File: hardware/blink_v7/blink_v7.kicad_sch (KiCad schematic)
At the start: 98 parts, among them J1 Conn_01x02, J14 Conn_02x16_Odd_Even, J5 Conn_01x04_Pin, J6 Conn_01x04_Pin, J7 Conn_01x06_Pin, J8 Conn_01x06, J9 USB_C_Receptacle, SW1 MK-12C02-G025, SW2 SW_SPDT, SW3 SW_SPDT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

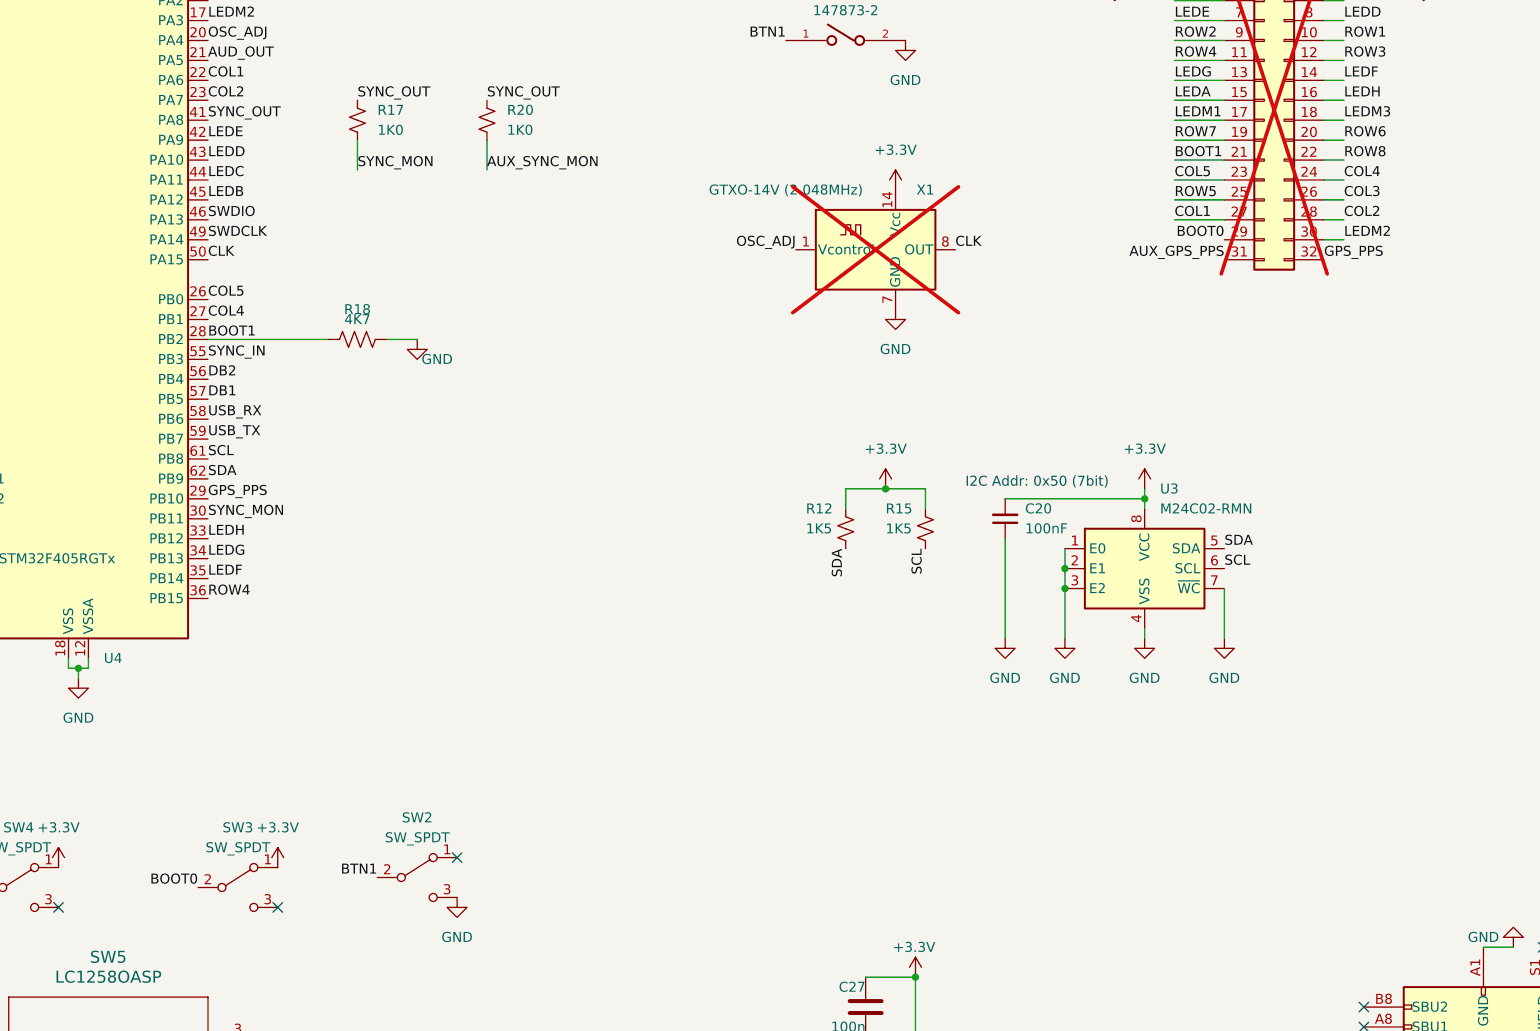
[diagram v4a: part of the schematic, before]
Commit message: main counter counting
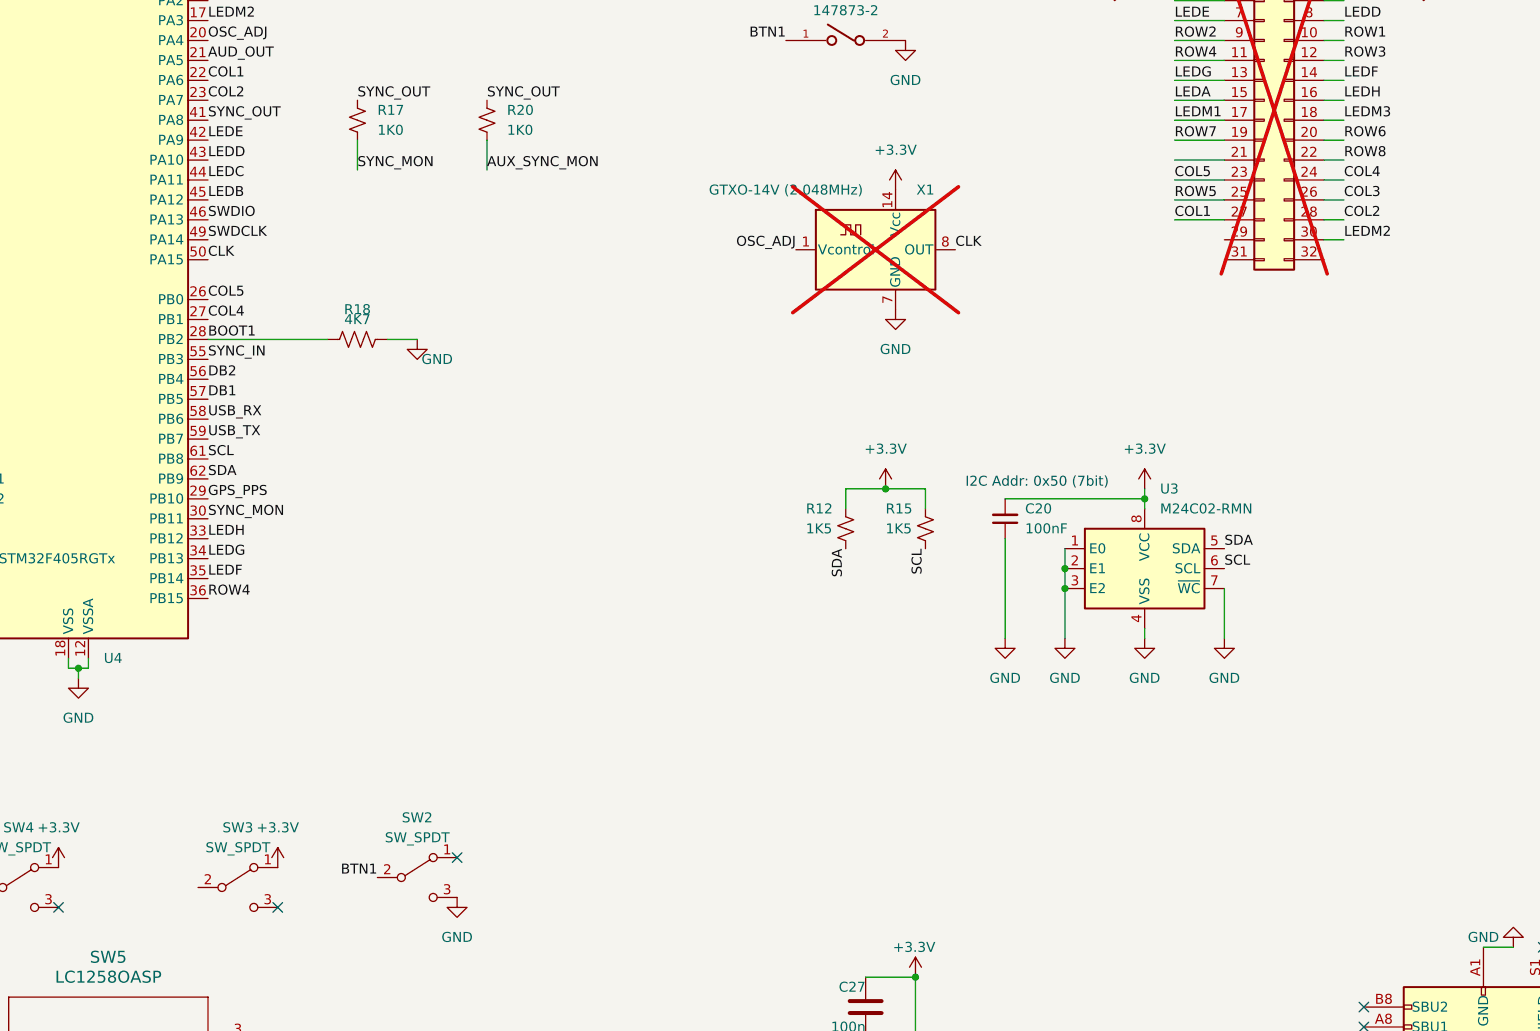
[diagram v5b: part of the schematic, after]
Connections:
- net AUX_GPS_PPS: no longer J14.31 (Pin_31)
- net BOOT0: no longer J14.29 (Pin_29), SW3.2 (B)
- net BOOT1: no longer J14.21 (Pin_21)
- net GPS_PPS: no longer J14.32 (Pin_32)
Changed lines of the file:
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@@
-    (effects (font (size 1.27 1.27)) (justify right bottom))
-  )
-  (label "AUX_GPS_PPS" (at 372.11 71.12 180) (fields_autoplaced)
     (effects (font (size 1.27 1.27)) (justify right bottom))
   )
@@
     (effects (font (size 1.27 1.27)) (justify left bottom))
   )
-  (label "BOOT0" (at 372.11 68.58 180) (fields_autoplaced)
-    (effects (font (size 1.27 1.27)) (justify right bottom))
-  )
   (label "DB3" (at 207.01 50.8 180) (fields_autoplaced)
     (effects (font (size 1.27 1.27)) (justify right bottom))
@@
     (effects (font (size 1.27 1.27)) (justify left bottom))
   )
-  (label "BOOT0" (at 241.3 151.13 180) (fields_autoplaced)
-    (effects (font (size 1.27 1.27)) (justify right bottom))
-  )
   (label "SYNC_IN2" (at 207.01 71.12 180) (fields_autoplaced)
     (effects (font (size 1.27 1.27)) (justify right bottom))
@@
     (effects (font (size 1.27 1.27)) (justify right bottom))
   )
-  (label "BOOT1" (at 365.76 58.42 0) (fields_autoplaced)
-    (effects (font (size 1.27 1.27)) (justify left bottom))
-  )
   (label "LEDB" (at 242.57 63.5 0) (fields_autoplaced)
     (effects (font (size 1.27 1.27)) (justify left bottom))
@@
     (effects (font (size 1.27 1.27)) (justify left bottom))
   )
-  (label "GPS_PPS" (at 384.81 71.12 0) (fields_autoplaced)
-    (effects (font (size 1.27 1.27)) (justify left bottom))
-  )

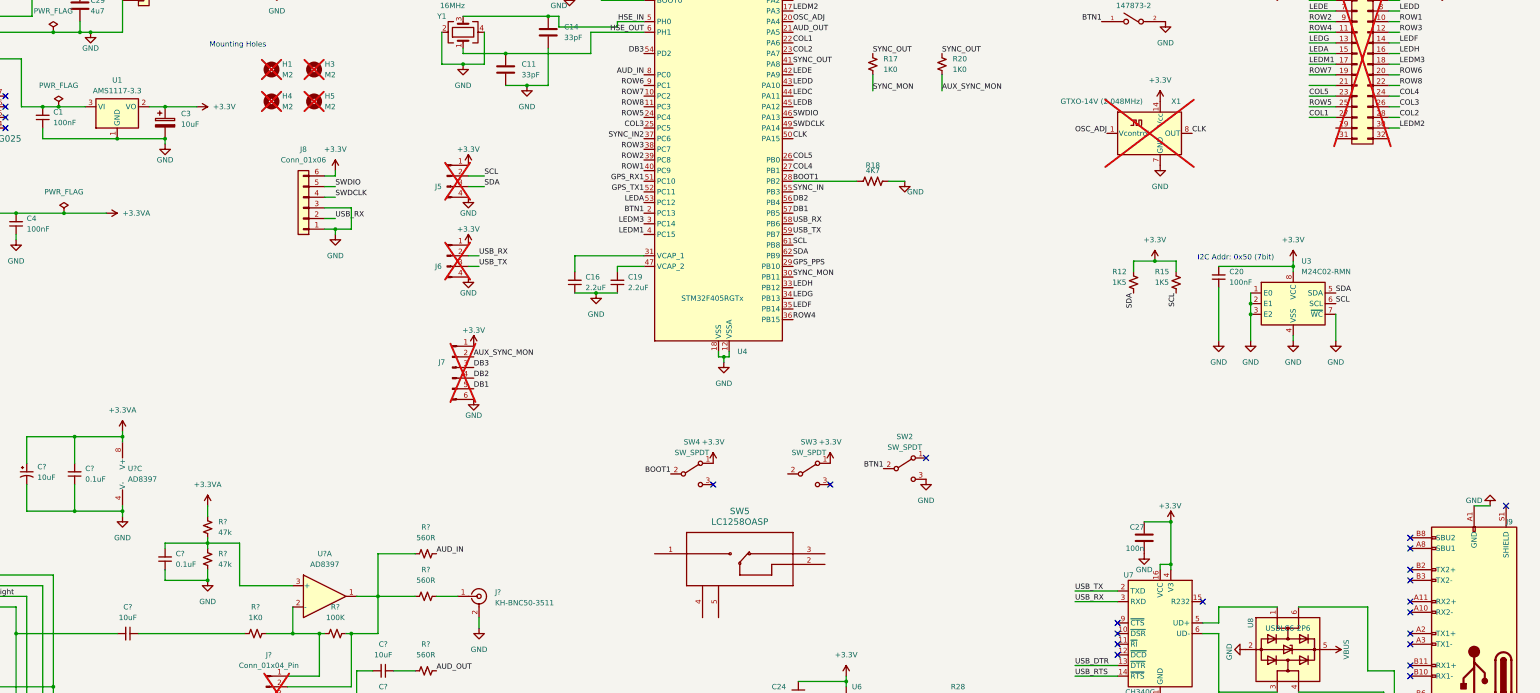
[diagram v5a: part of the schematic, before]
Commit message: add switches
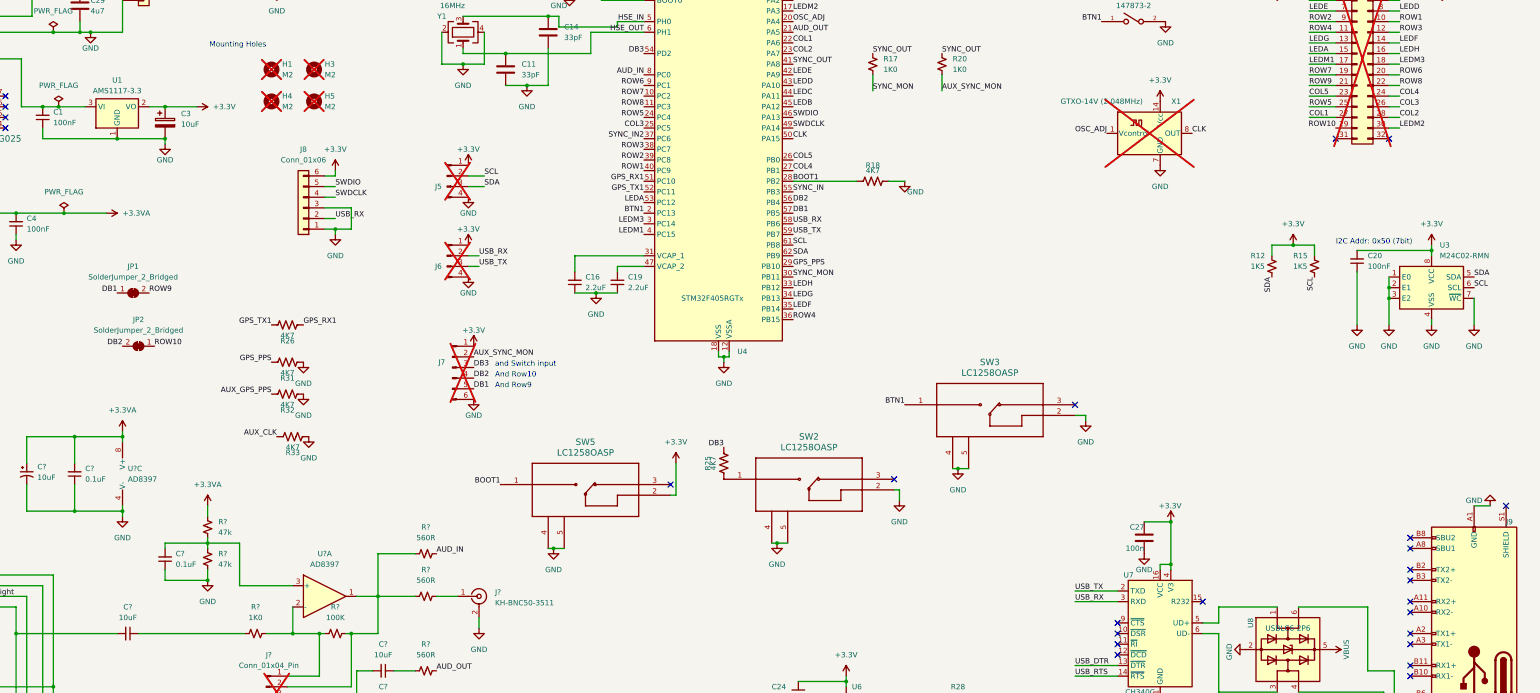
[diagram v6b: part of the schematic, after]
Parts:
- removed SW2, SW3, SW4: SW_SPDT, symbol Switch:SW_SPDT
- added JP1, JP2: SolderJumper_2_Bridged, Jumper:SolderJumper-2_P1.3mm_Bridged_RoundedPad1.0x1.5mm, symbol Jumper:SolderJumper_2_Bridged
- added R25, R26, R31, R32, R33: 4K7, Resistor_SMD:R_0603_1608Metric, symbol Device:R_US
- added SW2, SW3: LC1258OASP, blinky_footprints:LC1258OASP, symbol blinky:LC1258OASP
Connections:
- net +3.3V: now also SW5.2
- net AUX_CLK: now also R33.1
- net AUX_GPS_PPS: now also R32.1
- net BOOT1: now also SW5.1
- net BTN1: now also SW3.1
- net DB1: now also JP1.1 (A)
- net DB2: now also JP2.2 (B)
- net DB3: now also R25.1
- net GND: now also SW5.4, SW5.5, R31.2, R32.2, R33.2, SW2.2, SW2.4, SW2.5, SW3.2, SW3.4, SW3.5
- net GPS_PPS: now also R31.1
- net GPS_RX1: now also R26.2
- net GPS_TX1: now also R26.1
- net ROW9: now reaches J14.21 (Pin_21)
- net ROW9: now also JP1.2 (B)
- net ROW10: now reaches J14.29 (Pin_29)
- net ROW10: now also JP2.1 (A)
- new net: R25.2, SW2.1
- no-connect marks 24 -> 26
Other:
- note added: "And Row10"
- note added: "And Row9"
- note added: "and Switch input"
- moved on the sheet: C20, R12, R15, SW5, U3

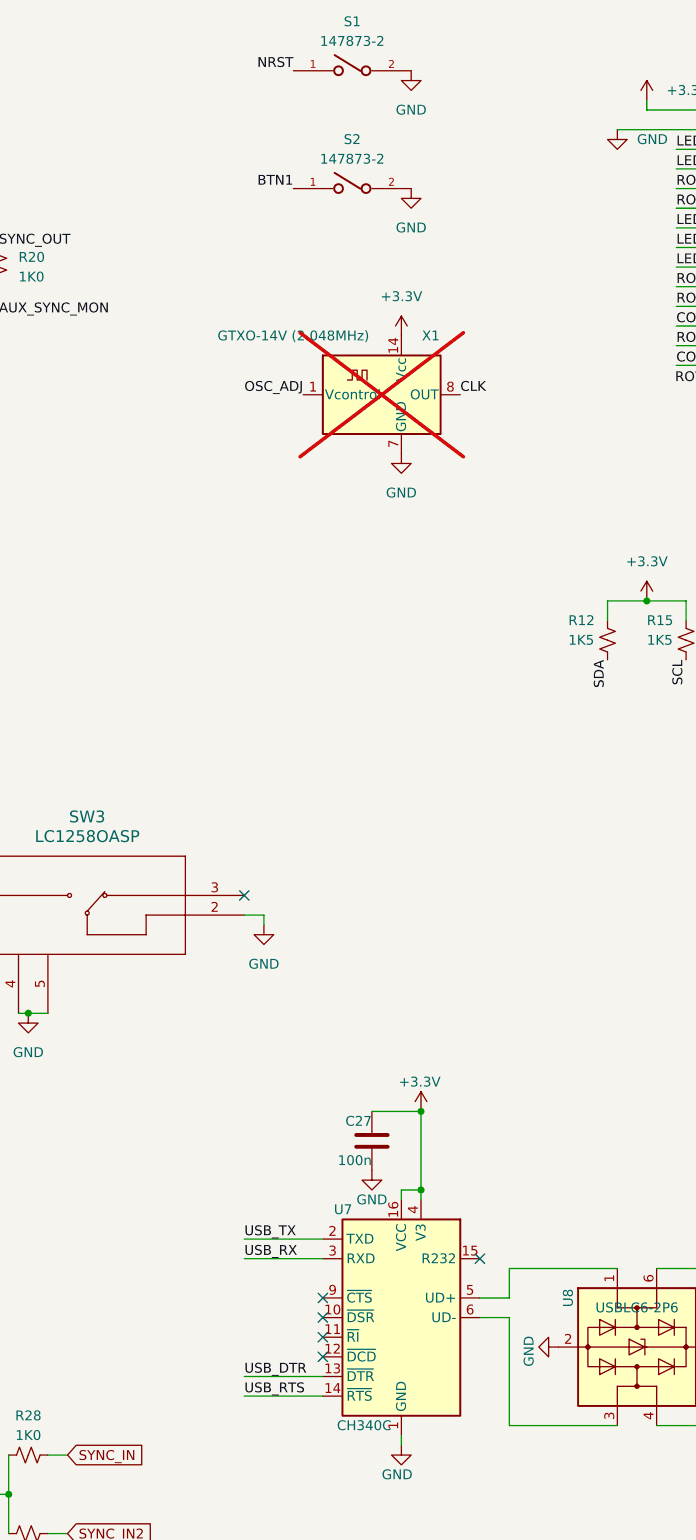
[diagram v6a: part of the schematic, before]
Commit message: update routing and boot switch
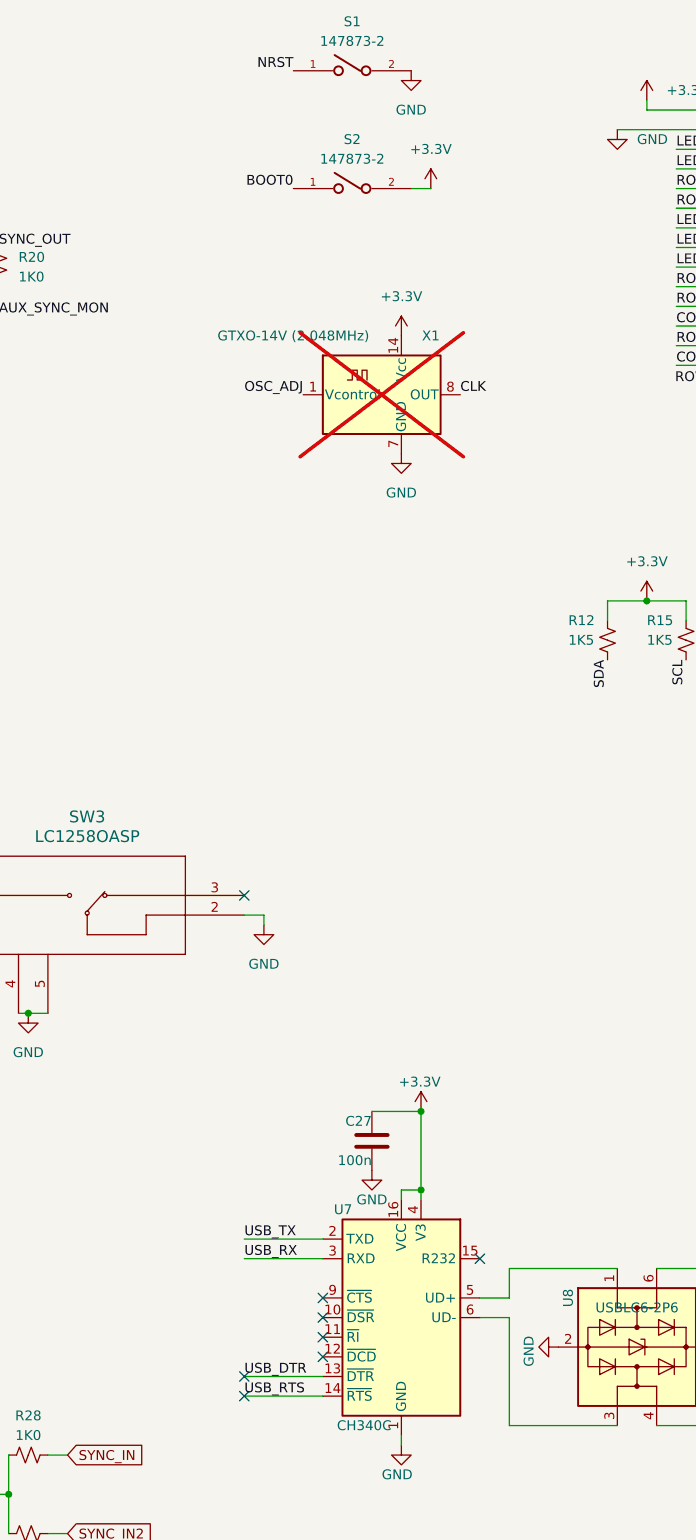
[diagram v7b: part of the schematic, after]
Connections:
- net +3.3V: now also S2.2
- net BOOT0: now also S2.1
- net BTN1: no longer S2.1
- net GND: no longer S2.2
- no-connect marks 26 -> 28
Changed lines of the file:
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@@
   (no_connect (at 54.61 68.58))
   (no_connect (at 389.89 196.85))
+  (no_connect (at 309.88 199.39))
   (no_connect (at 389.89 181.61))
   (no_connect (at 389.89 191.77))
@@
   (no_connect (at 213.36 153.67))
   (no_connect (at 54.61 66.04))
+  (no_connect (at 309.88 196.85))
   (no_connect (at 46.99 77.47))
   (no_connect (at 389.89 173.99))
@@
     (stroke (width 0) (type default))
   )
+  (wire (pts (xy 331.47 43.18) (xy 334.01 43.18))
+    (stroke (width 0) (type default))
+  )
   (wire (pts (xy 48.26 204.47) (xy 63.5 204.47))
     (stroke (width 0) (type default))
@@
     (effects (font (size 1.27 1.27)) (justify right bottom))
   )
-  (label "BTN1" (at 316.23 43.18 180) (fields_autoplaced)
-    (effects (font (size 1.27 1.27)) (justify right bottom))
-  )
   (label "ROW9" (at 365.76 58.42 0) (fields_autoplaced)
     (effects (font (size 1.27 1.27)) (justify left bottom))
@@
     (effects (font (size 1.27 1.27)) (justify right bottom))
   )
+  (label "BOOT0" (at 316.23 43.18 180) (fields_autoplaced)
+    (effects (font (size 1.27 1.27)) (justify right bottom))
+  )
   (label "USB_RX" (at 167.64 99.06 0) (fields_autoplaced)
     (effects (font (size 1.27 1.27)) (justify left bottom))
@@
     )
   )
-  (symbol (lib_id "power:GND") (at 331.47 43.18 0) (unit 1)
-    (in_bom yes) (on_board yes) (dnp no) (fields_autoplaced)
-    (property "Reference" "#PWR011" (at 331.47 49.53 0)
-      (effects (font (size 1.27 1.27)) hide)
-    )
-    (property "Value" "GND" (at 331.47 48.26 0)
-      (effects (font (size 1.27 1.27)))
-    )
-    (property "Footprint" "" (at 331.47 43.18 0)
-      (effects (font (size 1.27 1.27)) hide)
-    )
-    (property "Datasheet" "" (at 331.47 43.18 0)
-      (effects (font (size 1.27 1.27)) hide)
-    )
-    (pin "1")
-    (instances
-      (project "blink_v7"
-        (path "/bd4d3b9a-07c1-4a53-9c94-2893f3e869d4"
-          (reference "#PWR011") (unit 1)
-        )
-      )
-    )
-  )
   (symbol (lib_id "Oscillator:GTXO-14V") (at 330.2 69.85 0) (unit 1)
     (in_bom no) (on_board yes) (dnp yes)
@@
         )
       )
+    )
+  )
+  (symbol (lib_id "power:+3.3V") (at 334.01 43.18 0) (unit 1)
+    (in_bom yes) (on_board yes) (dnp no) (fields_autoplaced)
+    (property "Reference" "#PWR011" (at 334.01 46.99 0)
+      (effects (font (size 1.27 1.27)) hide)
+    )
+    (property "Value" "+3.3V" (at 334.01 38.1 0)
+      (effects (font (size 1.27 1.27)))
+    )
+    (property "Footprint" "" (at 334.01 43.18 0)
+      (effects (font (size 1.27 1.27)) hide)
+    )
+    (property "Datasheet" "" (at 334.01 43.18 0)
+      (effects (font (size 1.27 1.27)) hide)
+    )
+    (pin "1")
+    (instances
+      (project "blink_v7"
+        (path "/bd4d3b9a-07c1-4a53-9c94-2893f3e869d4"
+          (reference "#PWR011") (unit 1)
+        )
+      )
